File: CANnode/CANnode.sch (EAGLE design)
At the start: 240 parts, among them IC1 ISO1050DUB, IC2 ISO1050DUB, Q1 FDV302P, Q3 FDV302P, U1 LM324PW, U10 FT2232HL, U11 93LC56C-I/SN, U2 TPS70445_PWP_24, U3 LM324PW, U4 LM324PW, U5 LM324PW, U6 LM324PW, U7 RM42L432_PZ_100RM42L432_PZ_100, U8 LM324PW, U9 XC2C32A-6CP56C, X1 AS14-35, Y1 12M

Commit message: Changed 22R to 22, component names and rearranged wires
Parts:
- removed R88: TVS DIODE, eagle-ltspice:RR0402
- added D33, D35: TVS DIODE, eagle-ltspice:RR0402
- added H1, H2, H3, H4: MOUNT-HOLE5.5, holes:MOUNT-HOLE5.5
- R41, R42: value 22R -> 22
- R59: value TVS DIODE -> DNP; device eagle-ltspice:RR0402 -> resistor:R-US_R0402
- R96: value 200R -> 200
- renumbered R60 to D32, R80 to D30, R85 to D31, R87 to D34
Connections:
- new net CGND: R59.2
- net A7_IN: now also D33.2; no longer R59.2
- net D0_IN: now also D19.2
- net D1_IN: now also D20.2
- net D2_IN: now also D21.2
- net D3_IN: now also D34.2
- net D4_IN: now also D22.2
- net D5_IN: now also D23.2
- net D6_IN: now also D24.2
- net D7_IN: now also D35.2
- net GND: now also D13.1, D14.1, D15.1, D16.1, D17.1, D18.1, D19.1, D20.1, D21.1, D22.1, D23.1, D24.1, D31.1, D32.1, D33.1, D34.1, D35.1
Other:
- moved on the sheet: D24

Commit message: started layout experiment. its difficult and weird first attempt.
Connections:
- removed net N$10: D7.2, IC2.CANL, R6.1
- removed net N$11: D8.1, IC2.CANH, R6.2
- removed net N$8: D25.1, IC1.CANH, R5.2
- removed net N$9: D9.2, IC1.CANL, R5.1
- new net CAN1H: D25.1, IC1.CANH, R5.2, X1/3.1
- new net CAN1L: D9.2, IC1.CANL, R5.1, X1/4.1
- new net CAN2H: D8.1, IC2.CANH, R6.2, X1/5.1
- new net CAN2L: D7.2, IC2.CANL, R6.1, X1/6.1
- net CAN1RX: no longer X1/3.1
- net CAN1TX: no longer X1/4.1
- net CAN2RX: no longer X1/5.1
- net CAN2TX: no longer X1/6.1
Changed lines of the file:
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@@
-</segment>
-<segment>
-<pinref part="X1" gate="/4" pin="1"/>
-<wire x1="248.92" y1="-162.56" x2="241.3" y2="-162.56" width="0.1524" layer="91"/>
-<label x="233.68" y="-162.56" size="1.778" layer="95"/>
 </segment>
 <segment>
@@
 </segment>
 <segment>
-<pinref part="X1" gate="/6" pin="1"/>
-<wire x1="248.92" y1="-167.64" x2="241.3" y2="-167.64" width="0.1524" layer="91"/>
-<label x="233.68" y="-167.64" size="1.778" layer="95"/>
-</segment>
-<segment>
 <wire x1="256.54" y1="-81.28" x2="248.92" y2="-81.28" width="0.1524" layer="91"/>
 <label x="241.3" y="-81.28" size="1.778" layer="95"/>
@@
 </segment>
 <segment>
-<pinref part="X1" gate="/5" pin="1"/>
-<wire x1="241.3" y1="-165.1" x2="248.92" y2="-165.1" width="0.1524" layer="91"/>
-<label x="233.68" y="-165.1" size="1.778" layer="95"/>
-</segment>
-<segment>
 <wire x1="248.92" y1="-78.74" x2="256.54" y2="-78.74" width="0.1524" layer="91"/>
 <label x="241.3" y="-78.74" size="1.778" layer="95"/>
@@
 <wire x1="449.58" y1="-50.8" x2="449.58" y2="30.48" width="0.1524" layer="91"/>
 <pinref part="IC1" gate="G$1" pin="RXD"/>
-</segment>
-<segment>
-<pinref part="X1" gate="/3" pin="1"/>
-<wire x1="248.92" y1="-160.02" x2="241.3" y2="-160.02" width="0.1524" layer="91"/>
-<label x="233.68" y="-160.02" size="1.778" layer="95"/>
 </segment>
 <segment>
@@
 </segment>
 </net>
-<net name="N$8" class="0">
+<net name="CAN1H" class="0">
 <segment>
 <wire x1="505.46" y1="30.48" x2="523.24" y2="30.48" width="0.1524" layer="91"/>
@@
 <wire x1="533.4" y1="33.02" x2="533.4" y2="30.48" width="0.1524" layer="91"/>
 <junction x="533.4" y="30.48"/>
+<label x="541.02" y="30.48" size="1.778" layer="95"/>
+</segment>
+<segment>
+<pinref part="X1" gate="/3" pin="1"/>
+<wire x1="248.92" y1="-160.02" x2="241.3" y2="-160.02" width="0.1524" layer="91"/>
+<label x="233.68" y="-160.02" size="1.778" layer="95"/>
 </segment>
 </net>
-<net name="N$9" class="0">
+<net name="CAN1L" class="0">
 <segment>
 <wire x1="518.16" y1="27.94" x2="518.16" y2="20.32" width="0.1524" layer="91"/>
@@
 <wire x1="533.4" y1="20.32" x2="533.4" y2="17.78" width="0.1524" layer="91"/>
 <junction x="533.4" y="20.32"/>
+<label x="541.02" y="20.32" size="1.778" layer="95"/>
+</segment>
+<segment>
+<pinref part="X1" gate="/4" pin="1"/>
+<wire x1="248.92" y1="-162.56" x2="241.3" y2="-162.56" width="0.1524" layer="91"/>
+<label x="233.68" y="-162.56" size="1.778" layer="95"/>
 </segment>
 </net>
-<net name="N$10" class="0">
+<net name="CAN2L" class="0">
 <segment>
 <wire x1="502.92" y1="-45.72" x2="515.62" y2="-45.72" width="0.1524" layer="91"/>
@@
 <wire x1="533.4" y1="-55.88" x2="533.4" y2="-53.34" width="0.1524" layer="91"/>
 <junction x="533.4" y="-53.34"/>
+<label x="538.48" y="-53.34" size="1.778" layer="95"/>
+</segment>
+<segment>
+<pinref part="X1" gate="/6" pin="1"/>
+<wire x1="248.92" y1="-167.64" x2="241.3" y2="-167.64" width="0.1524" layer="91"/>
+<label x="233.68" y="-167.64" size="1.778" layer="95"/>
 </segment>
 </net>
-<net name="N$11" class="0">
+<net name="CAN2H" class="0">
 <segment>
 <wire x1="502.92" y1="-43.18" x2="520.7" y2="-43.18" width="0.1524" layer="91"/>
@@
 <wire x1="533.4" y1="-40.64" x2="533.4" y2="-43.18" width="0.1524" layer="91"/>
 <junction x="533.4" y="-43.18"/>
+<label x="538.48" y="-43.18" size="1.778" layer="95"/>
+</segment>
+<segment>
+<pinref part="X1" gate="/5" pin="1"/>
+<wire x1="241.3" y1="-165.1" x2="248.92" y2="-165.1" width="0.1524" layer="91"/>
+<label x="233.68" y="-165.1" size="1.778" layer="95"/>
 </segment>
 </net>

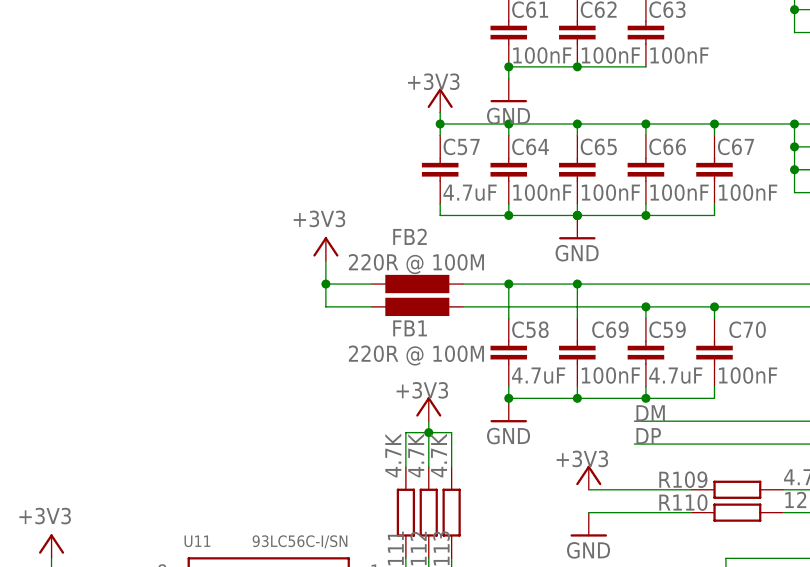
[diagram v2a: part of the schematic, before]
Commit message: Finished putting all the components on the board (but still needs to be more organized)
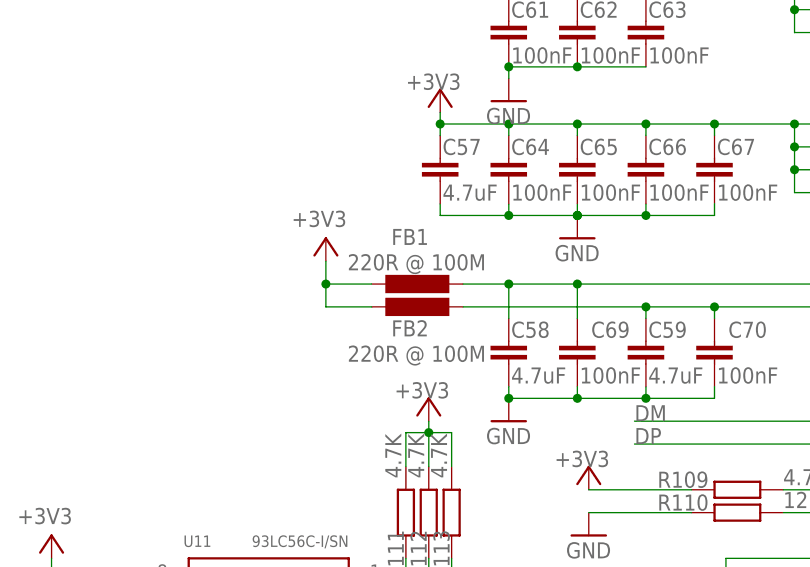
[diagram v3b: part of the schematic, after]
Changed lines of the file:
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@@
 </instance>
 <instance part="FB1" gate="G$1" x="104.14" y="-416.56" smashed="yes" rot="R90">
-<attribute name="NAME" x="105.41" y="-420.5986" size="1.778" layer="95" rot="R180"/>
+<attribute name="NAME" x="105.41" y="-410.4386" size="1.778" layer="95" rot="R180"/>
 <attribute name="VALUE" x="111.76" y="-413.258" size="1.778" layer="96" rot="R180"/>
 </instance>
 <instance part="FB2" gate="G$1" x="104.14" y="-419.1" smashed="yes" rot="R90">
-<attribute name="NAME" x="105.41" y="-410.4386" size="1.778" layer="95" rot="R180"/>
+<attribute name="NAME" x="105.41" y="-420.5986" size="1.778" layer="95" rot="R180"/>
 <attribute name="VALUE" x="111.76" y="-423.418" size="1.778" layer="96" rot="R180"/>
 </instance>
